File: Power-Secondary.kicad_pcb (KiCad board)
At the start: 2 copper layers, 120 x 130 mm, 53 parts, among them J1 AUXBatteryConn, J10 BPS +12V, J2 BPS SUPPLY, J4 JUMP START, J5 HORN CTRL, J6 DRV FAN CTRL, J7 HORN +12V, J8 DRIVER FAN +12V, J9 RADIOS +12V, K1 G5Q-1, K2 G5Q-1, K3 G5Q-1, SW1 Batt Check, SW2 BPS PWR CHECK, SW3 RADIO PWR CHECK

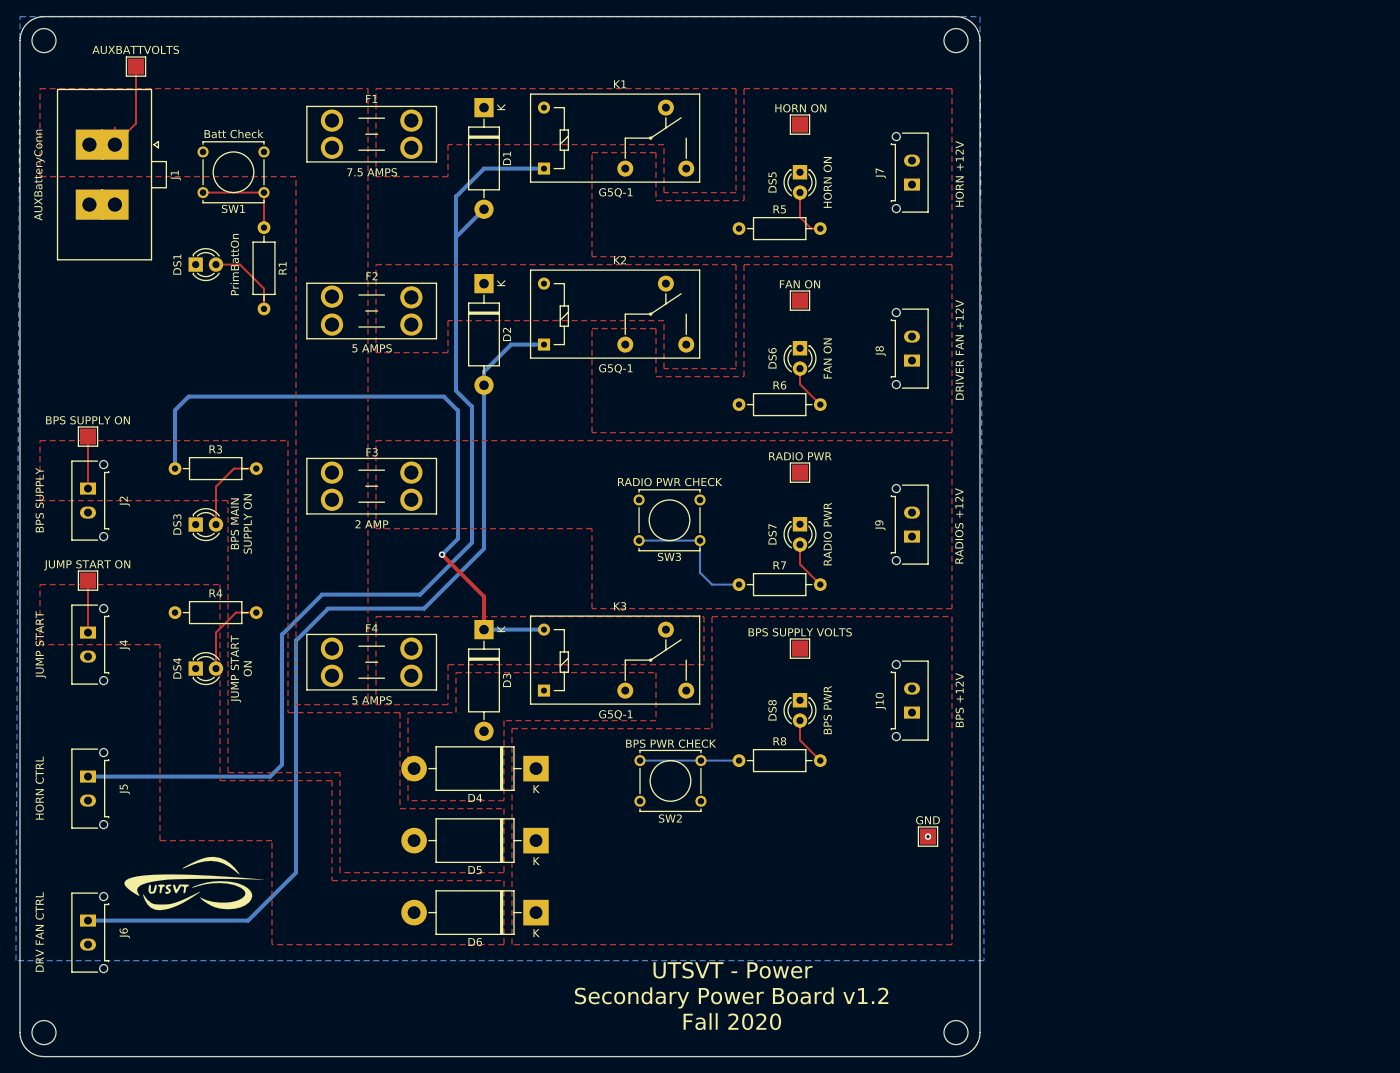
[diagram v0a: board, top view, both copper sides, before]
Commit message: secondary power pcb v2
Changed schematic, removed unnecessary/old files
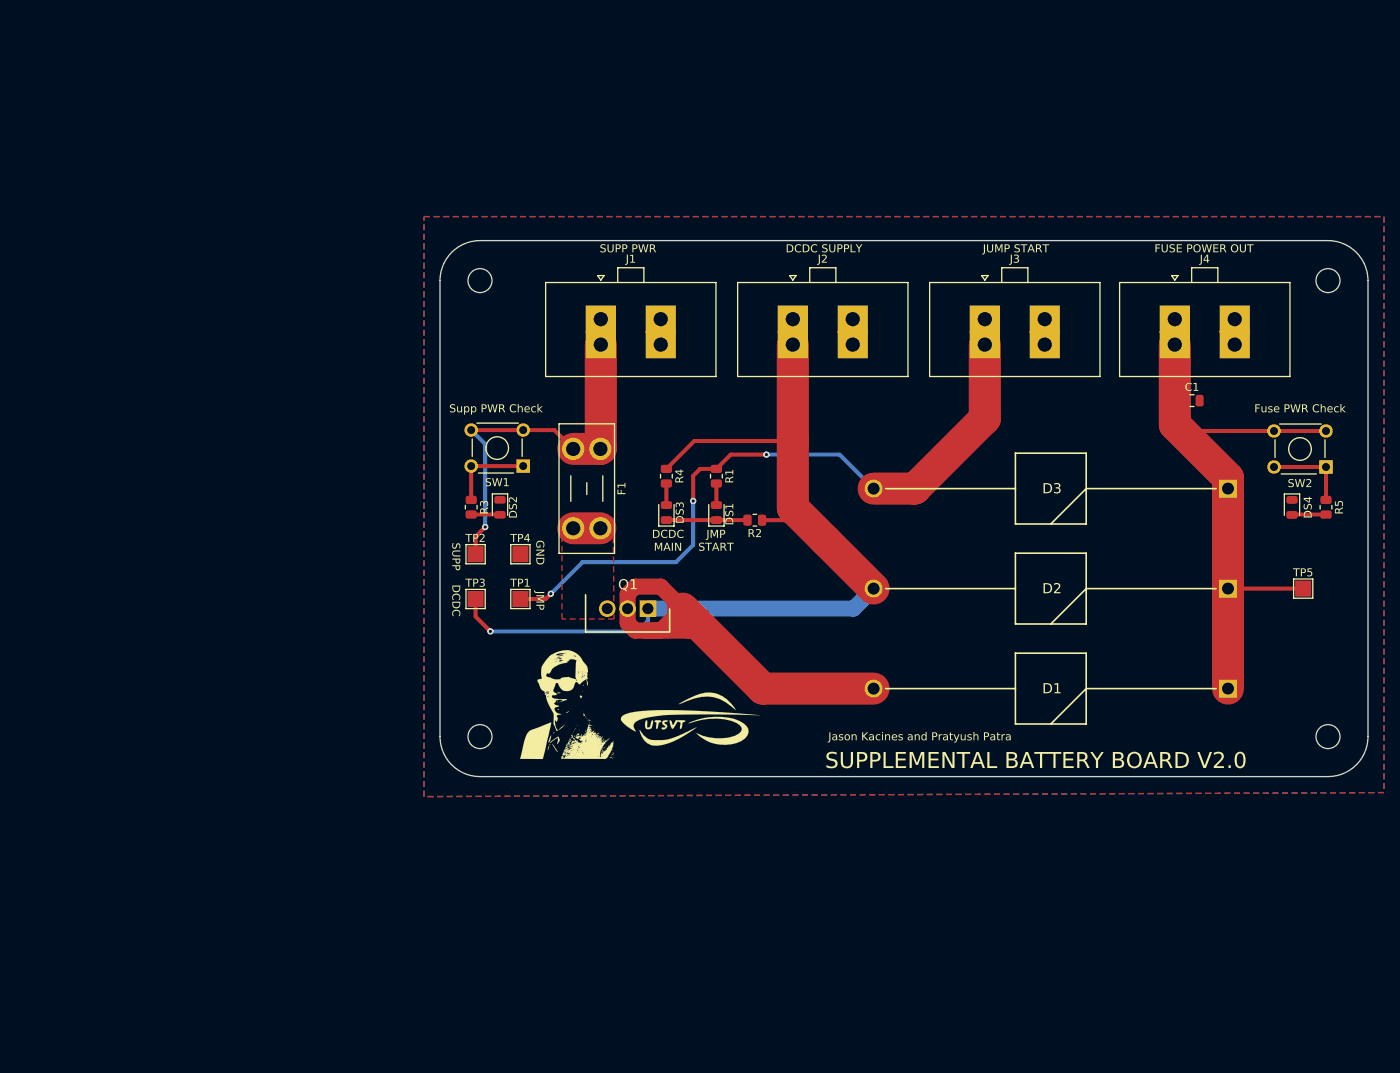
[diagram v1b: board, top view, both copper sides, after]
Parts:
- removed D4, D5, D6: SB5100-T, Diode_THT:D_DO-201AD_P15.24mm_Horizontal
- removed DS5: HORN ON, LED_THT:LED_D3.0mm
- removed DS6: FAN ON, LED_THT:LED_D3.0mm
- removed DS7: RADIO PWR, LED_THT:LED_D3.0mm
- removed DS8: BPS PWR, LED_THT:LED_D3.0mm
- removed F2, F4: 5 AMPS, Fuse:Fuseholder_Blade_Mini_Keystone_3568
- removed F3: 2 AMP, Fuse:Fuseholder_Blade_Mini_Keystone_3568
- removed J10: BPS +12V, Connector_Molex:Molex_Micro-Fit_3.0_43650-0215_1x02_P3.00mm_Vertical
- removed J5: HORN CTRL, Connector_Molex:Molex_Micro-Fit_3.0_43650-0215_1x02_P3.00mm_Vertical
- removed J6: DRV FAN CTRL, Connector_Molex:Molex_Micro-Fit_3.0_43650-0215_1x02_P3.00mm_Vertical
- removed J7: HORN +12V, Connector_Molex:Molex_Micro-Fit_3.0_43650-0215_1x02_P3.00mm_Vertical
- removed J8: DRIVER FAN +12V, Connector_Molex:Molex_Micro-Fit_3.0_43650-0215_1x02_P3.00mm_Vertical
- removed J9: RADIOS +12V, Connector_Molex:Molex_Micro-Fit_3.0_43650-0215_1x02_P3.00mm_Vertical
- removed K1, K2, K3: G5Q-1, Relay_THT:Relay_SPDT_Omron-G5Q-1
- removed R6, R7, R8: 11K, Resistor_THT:R_Axial_DIN0207_L6.3mm_D2.5mm_P10.16mm_Horizontal
- removed SW3: RADIO PWR CHECK, Button_Switch_THT:SW_Tactile_Straight_KSA0Axx1LFTR
- removed TP6: FAN ON, TestPoint:TestPoint_Pad_2.0x2.0mm
- removed TP7: RADIO PWR, TestPoint:TestPoint_Pad_2.0x2.0mm
- removed TP8: BPS SUPPLY VOLTS, TestPoint:TestPoint_Pad_2.0x2.0mm
- removed TP9: GND, TestPoint:TestPoint_Pad_2.0x2.0mm
- added C1: 10uF, Capacitor_SMD:C_0805_2012Metric, F.Cu at (181.0, 88.0)
- added DS2: SUPP PWR, Diode_SMD:D_0805_2012Metric, F.Cu at (94.5, 101.3)
- added J3: JUMP START, Connector_Molex:Molex_Sabre_43160-0102_1x02_P7.49mm_Vertical, F.Cu at (155.1, 81.0)
- added Q1: AUIRF4905, UTSVT_PowerSupp:TO254P465X1031X1954-3P, F.Cu at (113.0, 114.0)
- added R2: 100k, Resistor_SMD:R_0805_2012Metric, F.Cu at (126.3, 103.0)
- added TP2: SUPP SUPPLY VOLTS, TestPoint:TestPoint_Pad_2.0x2.0mm, F.Cu at (91.5, 107.2)
- D1, D2, D3: value 1N4001 -> V25PN60; footprint Diode_THT:D_DO-15_P12.70mm_Horizontal -> UTSVT_PowerSupp:DIOAD4425W130L885D885
- DS1: value PrimBattOn -> JUMP START ON; footprint LED_THT:LED_D3.0mm -> Diode_SMD:D_0805_2012Metric
- DS3: value BPS MAIN SUPPLY ON -> DCDC MAIN SUPPLY ON; footprint LED_THT:LED_D3.0mm -> Diode_SMD:D_0805_2012Metric
- DS4: value JUMP START ON -> FUSE PWR; footprint LED_THT:LED_D3.0mm -> Diode_SMD:D_0805_2012Metric
- F1: value 7.5 AMPS -> 20 AMPS
- J1: value AUXBatteryConn -> SUPP PWR
- J2: value BPS SUPPLY -> DCDC SUPPLY; footprint Connector_Molex:Molex_Micro-Fit_3.0_43650-0215_1x02_P3.00mm_Vertical -> Connector_Molex:Molex_Sabre_43160-0102_1x02_P7.49mm_Vertical
- J4: value JUMP START -> FUSE +12V; footprint Connector_Molex:Molex_Micro-Fit_3.0_43650-0215_1x02_P3.00mm_Vertical -> Connector_Molex:Molex_Sabre_43160-0102_1x02_P7.49mm_Vertical
- LOGO1: footprint UTSVT_Special:Hallock_Image -> UTSVT_Special:Hallock_Image_Tiny; moved to F.Cu
- R1, R3, R4, R5: value 11K -> 5.1K; footprint Resistor_THT:R_Axial_DIN0207_L6.3mm_D2.5mm_P10.16mm_Horizontal -> Resistor_SMD:R_0805_2012Metric
- SW1: value Batt Check -> SUPP PWR CHECK; footprint Button_Switch_THT:SW_Tactile_Straight_KSA0Axx1LFTR -> Button_Switch_THT:SW_TH_Tactile_Omron_B3F-10xx
- SW2: value BPS PWR CHECK -> FUSE PWR CHECK; footprint Button_Switch_THT:SW_Tactile_Straight_KSA0Axx1LFTR -> Button_Switch_THT:SW_TH_Tactile_Omron_B3F-10xx
- TP1: value AUXBATTVOLTS -> JUMP START VOLTS
- TP3: value BPS MAIN MAIN SUPPLY -> DCDC MAIN SUPPLY
- TP4: value JUMP START VOLTS -> GND
- TP5: value HORN ON -> FUSE SUPPLY VOLTS
- moved H4 164.7 mm to (198.0, 130.0)
- moved J4 140.5 mm to (178.8, 81.0), turned to 0 degrees
- moved DS4 138.5 mm to (193.5, 101.3), turned to -90 degrees
- moved D1 118.0 mm to (185.5, 124.0), turned to 180 degrees
- moved H3 105.4 mm to (92.0, 130.0)
- moved H2 104.9 mm to (198.0, 73.0)
- moved D2 100.5 mm to (185.5, 111.5), turned to 180 degrees
- moved D3 94.7 mm to (185.5, 99.0), turned to 180 degrees
- moved SW2 93.3 mm to (197.8, 96.3), turned to 180 degrees
- moved J2 89.9 mm to (131.1, 81.0), turned to 0 degrees
- moved TP5 85.6 mm to (194.9, 111.5)
- moved TP1 82.1 mm to (97.0, 112.8)
- moved R5 81.2 mm to (197.8, 101.3), turned to -90 degrees
- moved DS1 72.1 mm to (121.5, 102.0), turned to 90 degrees
- moved J1 68.6 mm to (107.1, 81.0), turned to 0 degrees
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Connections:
- D1 pad 1: Net-(D1-Pad1) -> Net-(C1-Pad1)
- D2 pad 1: Net-(D2-Pad1) -> Net-(C1-Pad1)
- D3 pad 1: Net-(D3-Pad1) -> Net-(C1-Pad1)
- D3 pad 2: GNDS -> Net-(D3-Pad2)
- F1 pad 2: Net-(D1-Pad1) -> Net-(F1-Pad2)
- J2 pad 1: Net-(D3-Pad1) -> Net-(D2-Pad2)
- J4 pad 1: Net-(D6-Pad2) -> Net-(C1-Pad1)
- R1 pad 1: Net-(R1-Pad1) -> Net-(D3-Pad2)
- R3 pad 1: Net-(D3-Pad1) -> Net-(R3-Pad1)
- R3 pad 2: Net-(DS3-Pad2) -> Net-(DS2-Pad2)
- R4 pad 1: Net-(D6-Pad2) -> Net-(D2-Pad2)
- R4 pad 2: Net-(DS4-Pad2) -> Net-(DS3-Pad2)
- R5 pad 1: Net-(J7-Pad1) -> Net-(R5-Pad1)
- R5 pad 2: Net-(DS5-Pad2) -> Net-(DS4-Pad2)
- SW1 pad 1: Net-(R1-Pad1) -> Net-(R3-Pad1)
- SW2 pad 1: Net-(R8-Pad1) -> Net-(R5-Pad1)
- SW2 pad 2: Net-(D4-Pad1) -> Net-(C1-Pad1)
- TP1 pad 1: Net-(F1-Pad1) -> Net-(D3-Pad2)
- TP3 pad 1: Net-(D3-Pad1) -> Net-(D2-Pad2)
- TP4 pad 1: Net-(D6-Pad2) -> GNDS
- TP5 pad 1: Net-(J7-Pad1) -> Net-(C1-Pad1)
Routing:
- net Net-(D3-Pad1): track 88.5 -> 0.00 mm, vias 1 -> 0
- net Net-(D3-Pad2): track 0.00 -> 85.2 mm, vias 0 -> 3
- net Net-(D1-Pad2): track 132.8 -> 55.2 mm
- net Net-(C1-Pad1): track 0.00 -> 75.3 mm
- net Net-(F1-Pad1): track 13.0 -> 46.9 mm, vias 0 -> 1
- net Net-(R7-Pad1): track 17.1 -> 0.00 mm
- net Net-(R8-Pad1): track 12.4 -> 0.00 mm
- net Net-(R1-Pad1): track 12.0 -> 0.00 mm
- net Net-(R3-Pad1): track 0.00 -> 10.7 mm
- net Net-(R5-Pad1): track 0.00 -> 10.6 mm
- net GNDS: track 0.25 -> 10.1 mm, vias 1 -> 0
- net Net-(DS3-Pad2): track 10.7 -> 2.70 mm
- net Net-(DS1-Pad2): track 9.78 -> 2.70 mm
- net Net-(D6-Pad2): track 6.50 -> 0.00 mm
- net Net-(DS4-Pad2): track 10.6 -> 4.27 mm
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- added copper zone on F.Cu, net GNDS
- added copper zone on F.Cu, net Net-(F1-Pad2)
- removed copper zone on F.Cu, net Net-(D1-Pad1)
- removed copper zone on F.Cu, net Net-(D2-Pad1)
- removed copper zone on F.Cu, net Net-(D3-Pad1)
- removed copper zone on F.Cu, net Net-(D4-Pad1)
- removed copper zone on F.Cu, net Net-(D4-Pad2)
- removed copper zone on F.Cu, net Net-(D6-Pad2)
- removed copper zone on F.Cu, net Net-(F1-Pad1)
- removed copper zone on F.Cu, net Net-(F3-Pad2)
- removed copper zone on F.Cu, net Net-(F4-Pad2)
- removed copper zone on F.Cu, net Net-(J7-Pad1)
- removed copper zone on F.Cu, net Net-(J8-Pad1)
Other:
- board size 120 x 130 mm -> 116 x 67 mm
- net class Default removed
- board text added: "DCDC"
- board text added: "DCDC MAIN"
- board text added: "DCDC SUPPLY"
- board text added: "FUSE POWER OUT"
- board text added: "Fuse PWR Check"
- board text added: "JMP"
- board text added: "JMP START"
- board text added: "JUMP START"
- board text added: "Jason Kacines and Pratyush Patra"
- board text added: "SUPP"
- board text added: "SUPP PWR"
- board text added: "SUPPLEMENTAL BATTERY BOARD V2.0"
- board text added: "Supp PWR Check"
- board text removed: "BPS MAIN SUPPLY ON"
- board text removed: "BPS SUPPLY ON"
- board text removed: "Dr. Gary Hallock"
- board text removed: "JUMP START ON"
- board text removed: "UTSVT - Power Secondary Power Board v1.2 Fall 2020"

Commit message: version 3
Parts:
- removed D1, D2, D3: V25PN60, UTSVT_PowerSupp:DIOAD4425W130L885D885
- removed F1: 20 AMPS, Fuse:Fuseholder_Blade_Mini_Keystone_3568
- removed J4: FUSE +12V, Connector_Molex:Molex_Sabre_43160-0102_1x02_P7.49mm_Vertical
- removed Q1: AUIRF4905, UTSVT_PowerSupp:TO254P465X1031X1954-3P
- removed SW1: SUPP PWR CHECK, Button_Switch_THT:SW_TH_Tactile_Omron_B3F-10xx
- removed SW2: FUSE PWR CHECK, Button_Switch_THT:SW_TH_Tactile_Omron_B3F-10xx
- added DS5: FUSE_OUT, Diode_SMD:D_0805_2012Metric, F.Cu at (146.1, 97.0)
- added Q1A1: SUP90P06-PCHANNEL-MOSFET, UTSVT_PowerSupp:SUP90P06-PCHAN-ENH-PWR-MOSFET, F.Cu at (141.5, 110.7)
- added Q2B1: SUP90P06-PCHANNEL-MOSFET, UTSVT_PowerSupp:SUP90P06-PCHAN-ENH-PWR-MOSFET, F.Cu at (162.4, 111.4)
- added R6: 100K, Resistor_SMD:R_0805_2012Metric, F.Cu at (172.1, 96.3)
- added R7: 5.1K, Resistor_SMD:R_0805_2012Metric, F.Cu at (163.3, 118.1)
- added R8: 5.1K, Resistor_SMD:R_0805_2012Metric, F.Cu at (146.1, 101.0)
- added TP6: GND, TestPoint:TestPoint_Pad_2.0x2.0mm, F.Cu at (131.7, 119.1)
- added U1: Opamp_Dual, UTSVT_PowerSupp:LM358P-OPAMP, F.Cu at (137.0, 99.8)
- DS1: value JUMP START ON -> SUPP_PWR
- DS2: value SUPP PWR -> DCDC_PWR
- DS3: value DCDC MAIN SUPPLY ON -> SUPP_GATE
- DS4: value FUSE PWR -> DCDC_GATE
- J3: value JUMP START -> FUSE +12V
- R2: value 100k -> 5.1K
- R4: value 5.1K -> 10K
- R5: value 5.1K -> 180K
- TP1: value JUMP START VOLTS -> SUPP_PWR
- TP2: value SUPP SUPPLY VOLTS -> DCDC_PWR
- TP3: value DCDC MAIN SUPPLY -> SUPP_GATE
- TP4: value GND -> DCDC_GATE
- TP5: value FUSE SUPPLY VOLTS -> FUSE_OUT
- moved TP2 91.1 mm to (181.2, 91.9)
- moved DS2 79.1 mm to (173.0, 91.6), turned to 0 degrees
- moved TP4 62.8 mm to (158.9, 118.1)
- moved R5 61.8 mm to (136.5, 92.8), turned to 0 degrees
- moved LOGO2 59.8 mm to (177.3, 120.3)
- moved TP3 53.6 mm to (144.8, 118.1)
- moved R3 52.4 mm to (140.6, 118.1), turned to 180 degrees
- moved R2 51.9 mm to (177.0, 91.6)
- moved TP5 51.9 mm to (146.3, 93.3)
- moved J2 51.3 mm to (178.2, 101.5), turned to -90 degrees
- moved LOGO1 50.3 mm to (151.3, 114.3)
- moved J1 32.3 mm to (123.3, 109.0), turned to 90 degrees
- moved TP1 31.2 mm to (127.6, 119.1)
- moved DS4 31.1 mm to (167.3, 118.1), turned to 180 degrees
- moved C1 29.5 mm to (157.8, 106.3)
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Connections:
- C1 pad 1: Net-(C1-Pad1) -> FUSE_OUT
- J1 pad 1: Net-(F1-Pad1) -> SUPP_PWR
- J2 pad 1: Net-(D2-Pad2) -> DCDC_PWR
- J3 pad 1: Net-(D3-Pad2) -> FUSE_OUT
- R1 pad 1: Net-(D3-Pad2) -> SUPP_PWR
- R2 pad 1: Net-(D2-Pad2) -> DCDC_PWR
- R2 pad 2: GNDS -> Net-(DS2-Pad2)
- R3 pad 1: Net-(R3-Pad1) -> SUPP_GATE
- R3 pad 2: Net-(DS2-Pad2) -> Net-(DS3-Pad2)
- R4 pad 1: Net-(D2-Pad2) -> SUPP_PWR
- R4 pad 2: Net-(DS3-Pad2) -> V_REF
- R5 pad 1: Net-(R5-Pad1) -> V_REF
- R5 pad 2: Net-(DS4-Pad2) -> GNDS
- TP1 pad 1: Net-(D3-Pad2) -> SUPP_PWR
- TP2 pad 1: Net-(F1-Pad1) -> DCDC_PWR
- TP3 pad 1: Net-(D2-Pad2) -> SUPP_GATE
- TP4 pad 1: GNDS -> DCDC_GATE
- TP5 pad 1: Net-(C1-Pad1) -> FUSE_OUT
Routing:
- net GNDS: track 10.1 -> 170.8 mm, vias 0 -> 1
- net Net-(D2-Pad2): track 116.7 -> 0.00 mm, vias 1 -> 0
- net Net-(D3-Pad2): track 85.2 -> 0.00 mm, vias 3 -> 0
- net FUSE_OUT: track 0.00 -> 83.9 mm
- net DCDC_PWR: track 0.00 -> 76.2 mm
- net Net-(C1-Pad1): track 75.3 -> 0.00 mm
- net Net-(D1-Pad2): track 55.2 -> 0.00 mm
- net Net-(F1-Pad1): track 46.9 -> 0.00 mm, vias 1 -> 0
- net SUPP_PWR: track 0.00 -> 46.9 mm, vias 0 -> 1
- net DCDC_GATE: track 0.00 -> 43.9 mm, vias 0 -> 1
- net SUPP_GATE: track 0.00 -> 18.1 mm, vias 0 -> 1
- net V_REF: track 0.00 -> 15.9 mm
- net Net-(R3-Pad1): track 10.7 -> 0.00 mm
- net Net-(R5-Pad1): track 10.6 -> 0.00 mm
- net Net-(F1-Pad2): track 3.40 -> 0.00 mm
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- removed copper zone on B.Cu, net GNDS
- removed copper zone on F.Cu, net GNDS
- removed copper zone on F.Cu, net Net-(F1-Pad2)
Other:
- board size 116 x 67 mm -> 84 x 38 mm
- board text added: "DCDC GATE"
- board text added: "DCDC PWR"
- board text added: "FUSE OUT"
- board text added: "FUSE PWR"
- board text added: "SUPP GATE"
- board text added: "SUPPLEMENTAL POWER BOARD v3.0 JASON AND PRATYUSH"
- board text removed: "DCDC"
- board text removed: "DCDC MAIN"
- board text removed: "DCDC SUPPLY"
- board text removed: "FUSE POWER OUT"
- board text removed: "Fuse PWR Check"
- board text removed: "JMP"
- board text removed: "JMP START"
- board text removed: "JUMP START"
- board text removed: "Jason Kacines and Pratyush Patra"
- board text removed: "SUPP"
- board text removed: "SUPPLEMENTAL BATTERY BOARD V2.0"
- board text removed: "Supp PWR Check"

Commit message: v3 update
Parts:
- LOGO1: moved to B.Cu
- moved LOGO1 7.18 mm to (158.0, 117.0), turned to 180 degrees
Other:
- board text added: "{dblquote}Rabid{dblquote}, not rabbit."

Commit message: v3 revision
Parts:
- added F1: Fuse, Fuse:Fuseholder_Blade_Mini_Keystone_3568, F.Cu at (159.7, 104.4)
- added J2: SUPP PWR 2, Connector_Molex:Molex_Sabre_43160-0102_1x02_P7.49mm_Vertical, F.Cu at (122.7, 88.0)
- J1: value SUPP PWR -> SUPP PWR 1
- moved LOGO2 57.5 mm to (141.4, 75.5)
- moved LOGO1 48.5 mm to (132.9, 75.5)
- moved TP6 47.4 mm to (178.9, 124.0)
- moved TP2 36.4 mm to (163.9, 123.9), turned to 180 degrees
- moved R4 33.6 mm to (168.1, 124.0), turned to 0 degrees
- moved DS2 32.5 mm to (172.1, 124.0), turned to 180 degrees
- moved R8 30.2 mm to (161.4, 75.0), turned to 180 degrees
- moved TP5 26.8 mm to (165.9, 75.0)
- moved J4 26.6 mm to (172.9, 80.2), turned to -90 degrees
- moved C1 25.0 mm to (165.4, 82.5), turned to -90 degrees
- moved DS5 24.6 mm to (156.9, 75.0), turned to 0 degrees
- moved H1 19.5 mm to (109.9, 71.0)
- moved H2 19.5 mm to (185.9, 71.0)
- moved R5 13.6 mm to (166.9, 108.9), turned to -90 degrees
- moved DS4 12.3 mm to (156.4, 124.0)
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- renumbered J2 to J3, J3 to J4, R4 to R2, R5 to R3, R2 to R4, R6 to R5, R3 to R6
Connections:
- Q2B1 pad 3: DCDC_PWR -> Net-(F1-Pad1)
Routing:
- net GNDS: track 170.8 -> 120.2 mm, vias 1 -> 0
- net FUSE_OUT: track 83.9 -> 134.2 mm
- net SUPP_PWR: track 46.9 -> 78.1 mm, vias 1 -> 0
- net Net-(F1-Pad1): track 0.00 -> 14.1 mm
- net DCDC_PWR: track 76.2 -> 81.5 mm, vias 0 -> 1
- net DCDC_GATE: track 43.9 -> 48.2 mm
- net SUPP_GATE: track 18.1 -> 21.3 mm
- net V_REF: track 15.9 -> 17.8 mm
- net Net-(DS5-Pad2): track 2.15 -> 2.65 mm
- added copper zone on B.Cu, net GNDS
- added copper zone on F.Cu, net GNDS
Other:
- board size 84 x 38 mm -> 83 x 60 mm
- board text added: "SUPP PWR 1"
- board text added: "SUPP PWR 2"
